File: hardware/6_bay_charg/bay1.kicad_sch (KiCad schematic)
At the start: 6 parts, among them Q1 AO4407A, Q2 DMG2302U, U2 TCA9803

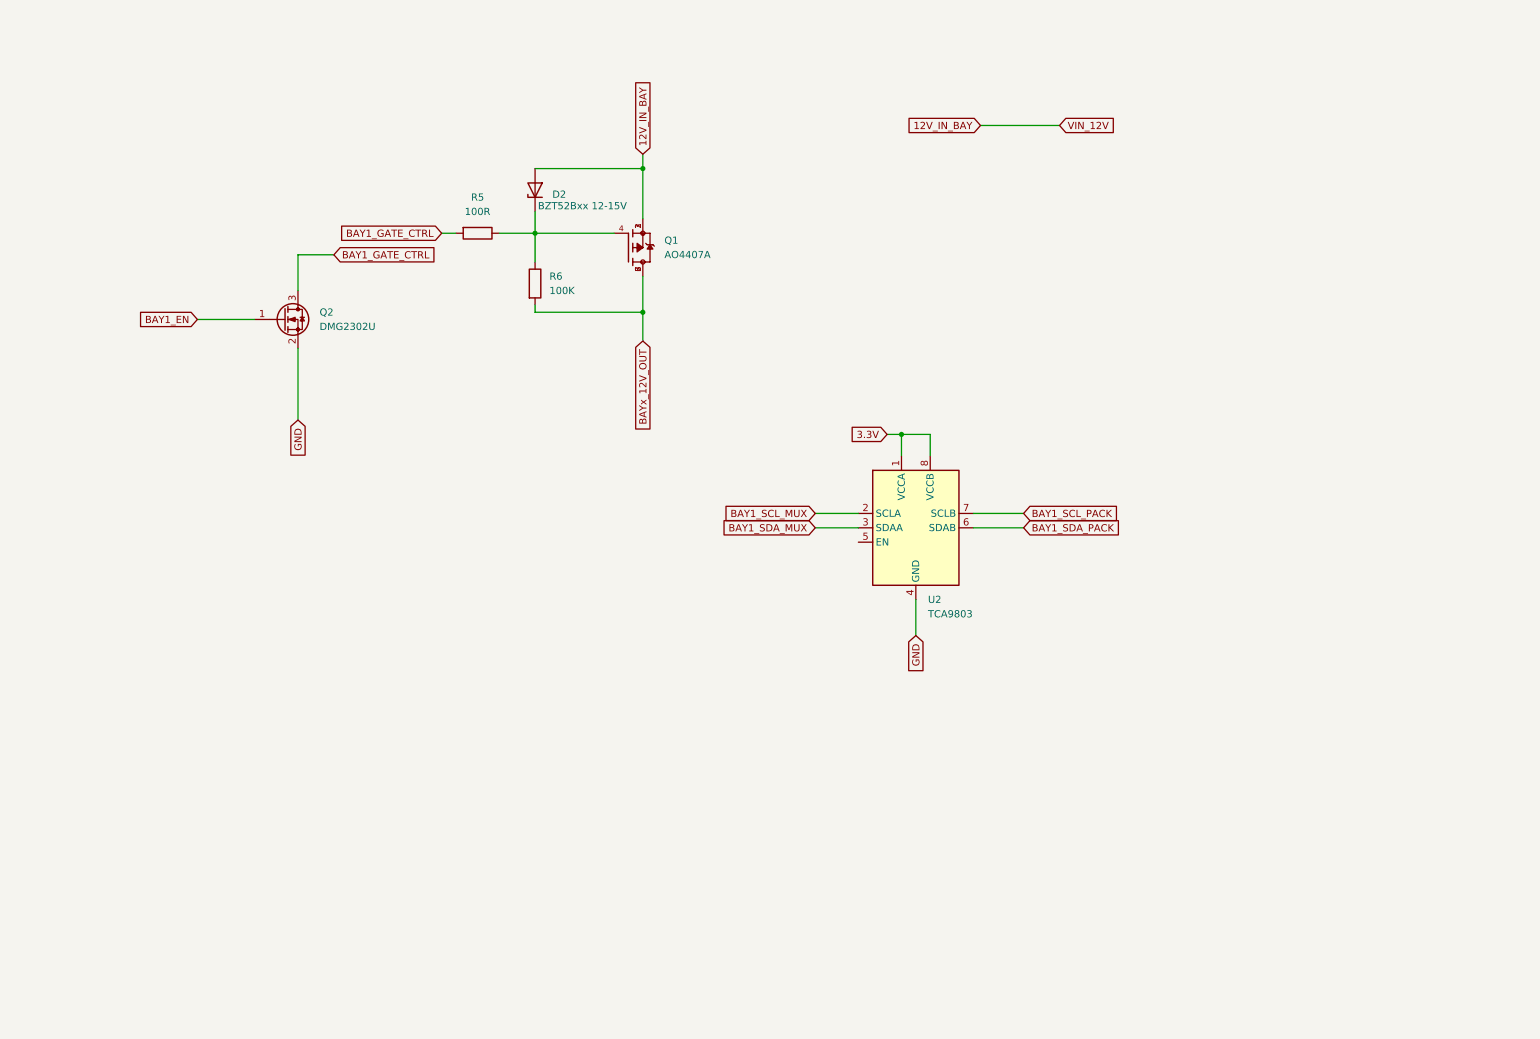
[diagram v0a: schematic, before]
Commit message: Update KiCad schematics: dual GPIO charge/discharge per bay
- Refactored bay power control logic
- Separated GPIOs for charge and discharge paths
- Added safe idle state with hardware interlock
- Improved overall safety and control clarity
- Updated and exported schematic PDF plots
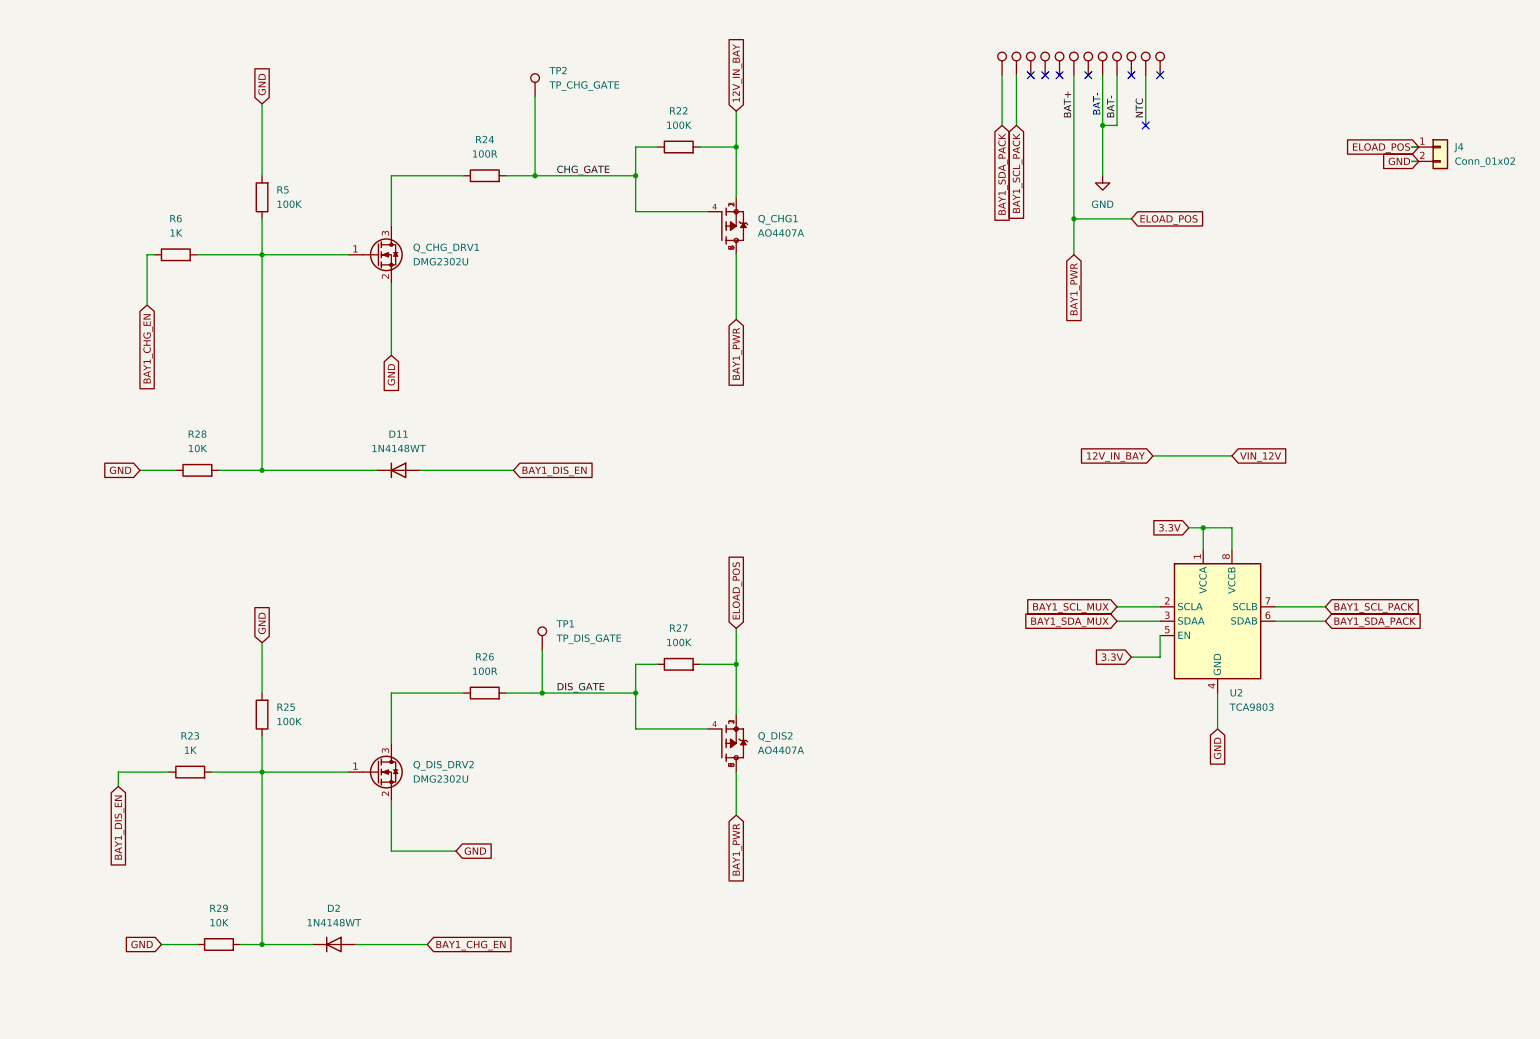
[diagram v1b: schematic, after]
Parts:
- removed D2: BZT52Bxx 12-15V, Diode_SMD:D_SOD-123F, symbol Diode:BZT52Bxx
- removed Q2: DMG2302U, Package_TO_SOT_SMD:SOT-23, symbol Transistor_FET:DMG2302U
- added D11, D2: 1N4148WT, Diode_SMD:D_SOD-523, symbol Diode:1N4148WT
- added J4: Conn_01x02, TerminalBlock_Phoenix:TerminalBlock_Phoenix_MKDS-1,5-2-5.08_1x02_P5.08mm_Horizontal, symbol Connector_Generic:Conn_01x02
- added Q_CHG_DRV1, Q_DIS_DRV2: DMG2302U, Package_TO_SOT_SMD:SOT-23, symbol Transistor_FET:DMG2302U
- added Q_DIS2: AO4407A, AO4407A:SOIC127P600X175-8N, symbol AO4407A:AO4407A
- added R22, R25, R27: 100K, symbol Device:R
- added R23: 1K, symbol Device:R
- added R24, R26: 100R, symbol Device:R
- added R28, R29: 10K, symbol Device:R
- added TP1: TP_DIS_GATE, symbol Connector:TestPoint
- added TP10, TP11, TP12, TP13, TP14, TP15, TP16, TP17, TP6, TP7, TP8, TP9: TestPoint, TestPoint:TestPoint_Pad_D2.3mm, symbol Connector:TestPoint
- added TP2: TP_CHG_GATE, symbol Connector:TestPoint
- R5: value 100R -> 100K
- R6: value 100K -> 1K
- renumbered Q1 to Q_CHG1
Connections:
- net BAY1_GATE_CTRL is gone; now on net GND: R5.2
- net 12V_IN_BAY: now also R22.2
- net 3.3V: now also U2.5 (EN)
- net BAY1_SCL_PACK: now also TP7.1
- net BAY1_SDA_PACK: now also TP6.1
- net GND: now also J4.2 (Pin_2), Q_CHG_DRV1.2 (S), Q_DIS_DRV2.2 (S), R25.2, R28.1, R29.1, TP13.1, TP14.1
- net BAYx_12V_OUT renamed BAY1_PWR
- net BAY1_PWR: now also J4.1 (Pin_1), Q_DIS2.1, Q_DIS2.2, Q_DIS2.3, Q_DIS2.5, Q_DIS2.6, Q_DIS2.7, Q_DIS2.8, R27.2, TP11.1; no longer R6.2
- new net: D11.1 (K), Q_CHG_DRV1.1 (G), R28.2, R5.1, R6.2
- new net: Q_CHG_DRV1.3 (D), R24.1
- new net: D2.1 (K), Q_DIS_DRV2.1 (G), R23.2, R25.1, R29.2
- new net: Q_DIS_DRV2.3 (D), R26.1
- new net BAY1_CHG_EN: D2.2 (A), R6.1
- new net BAY1_DIS_EN: D11.2 (A), R23.1
- new net CHG_GATE: Q_CHG1.4, R22.1, R24.2, TP2.1
- new net DIS_GATE: Q_DIS2.4, R26.2, R27.1, TP1.1
- new net NTC: TP16.1
- no-connect marks 0 -> 7
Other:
- note added: "BAT-"
- moved on the sheet: Q_CHG1, U2

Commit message: Integrate fan, USB interface, firmware, and cleaned KiCad schematics
- Added 12V fan for thermal management
- Integrated USB interface (hardware and firmware)
- Added initial firmware implementation
- Cleaned and refactored KiCad schematics
- Updated and regenerated schematic PDF plots
- Updated project README to reflect latest architecture
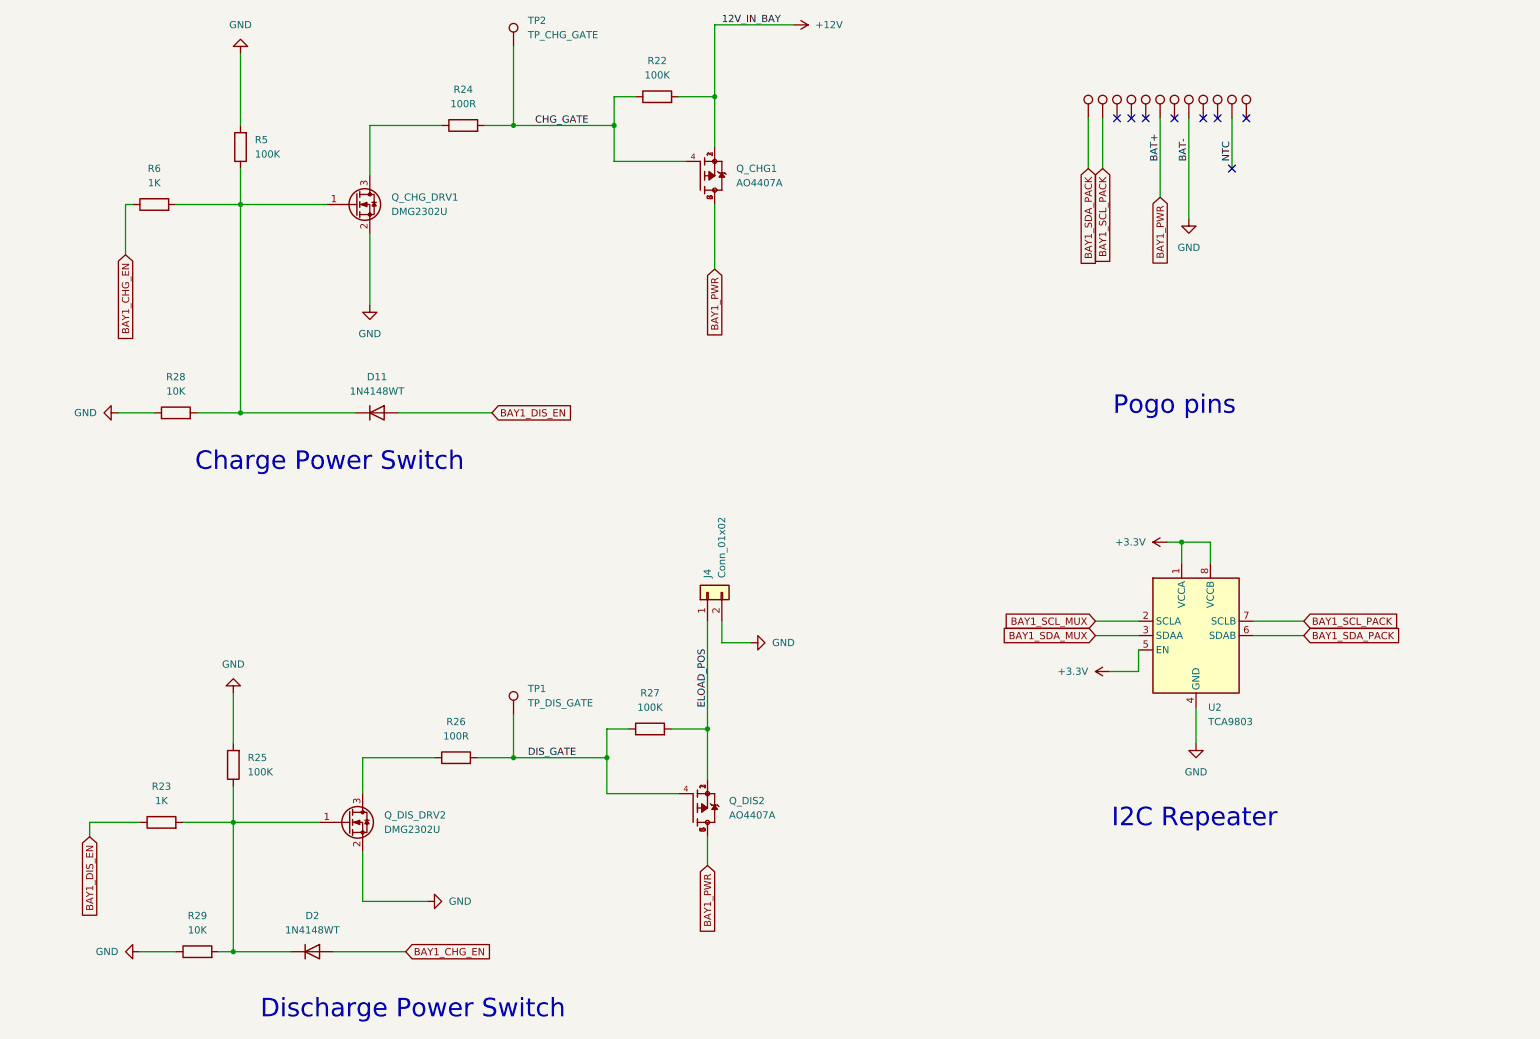
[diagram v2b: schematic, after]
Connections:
- net BAY1_PWR: no longer J4.1 (Pin_1), Q_DIS2.1, Q_DIS2.2, Q_DIS2.3, R27.2
- net GND: no longer TP14.1
- net 12V_IN_BAY renamed +12V
- net 3.3V renamed +3.3V
- new net ELOAD_POS: J4.1 (Pin_1), Q_DIS2.1, Q_DIS2.2, Q_DIS2.3, R27.2
- no-connect marks 7 -> 8
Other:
- note added: "Charge Power Switch"
- note added: "Discharge Power Switch"
- note added: "I2C Repeater"
- note added: "Pogo pins"
- note removed: "BAT-"
- moved on the sheet: D11, D2, J4, Q_CHG1, Q_CHG_DRV1, Q_DIS2, Q_DIS_DRV2, R22, R23, R24, R25, R26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

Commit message: updating FSM diagramme
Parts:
- J4: value Conn_01x02 -> ELOAD
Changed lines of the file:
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@@
 	(text "Pogo pins\n"
 		(exclude_from_sim no)
-		(at 219.71 86.36 0)
+		(at 220.472 74.676 0)
 		(effects
 			(font
@@
 	(wire
 		(pts
-			(xy 27.94 160.02) (xy 27.94 162.56)
-		)
-		(stroke
-			(width 0)
-			(type default)
-		)
-	)
-	(wire
-		(pts
 			(xy 137.16 143.51) (xy 137.16 152.4)
 		)
@@
 	(wire
 		(pts
-			(xy 34.29 50.8) (xy 34.29 59.69)
-		)
-		(stroke
-			(width 0)
-			(type default)
-		)
-	)
-	(wire
-		(pts
 			(xy 76.2 173.99) (xy 76.2 165.1)
 		)
@@
 	(wire
 		(pts
-			(xy 35.56 50.8) (xy 34.29 50.8)
+			(xy 35.56 50.8) (xy 31.75 50.8)
 		)
 		(stroke
@@
 	(wire
 		(pts
-			(xy 36.83 160.02) (xy 27.94 160.02)
+			(xy 36.83 160.02) (xy 31.75 160.02)
 		)
 		(stroke
@@
 	(global_label "BAY1_CHG_EN"
 		(shape input)
-		(at 34.29 59.69 270)
+		(at 31.75 50.8 180)
 		(fields_autoplaced yes)
 		(effects
@@
 		)
 		(property "Intersheetrefs" "${INTERSHEET_REFS}"
-			(at 34.29 75.6171 90)
+			(at 15.8229 50.8 0)
 			(effects
 				(font
@@
 	(global_label "BAY1_DIS_EN"
 		(shape input)
-		(at 27.94 162.56 270)
+		(at 31.75 160.02 180)
 		(fields_autoplaced yes)
 		(effects
@@
 		)
 		(property "Intersheetrefs" "${INTERSHEET_REFS}"
-			(at 27.94 177.7009 90)
+			(at 16.6091 160.02 0)
 			(effects
 				(font
@@
 			)
 		)
-		(property "Value" "Conn_01x02"
+		(property "Value" "ELOAD"
 			(at 139.6999 116.84 0)
 			(effects
